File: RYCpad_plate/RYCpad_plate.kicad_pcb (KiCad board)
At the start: 2 copper layers, 77.2 x 96.2 mm, 0 parts

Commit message: update plate "PCB" and produce gerber
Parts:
- added svg2mod (x2): G***, personal:RYCpad_plate_coppertrim, F.Cu at (0.00, 9.50)
- added svg2mod (x2): G***, personal:RYCpad_plate_coppertrim, B.Cu at (0.00, 9.50)
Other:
- board text added: "RYCpad Plate v1.0"

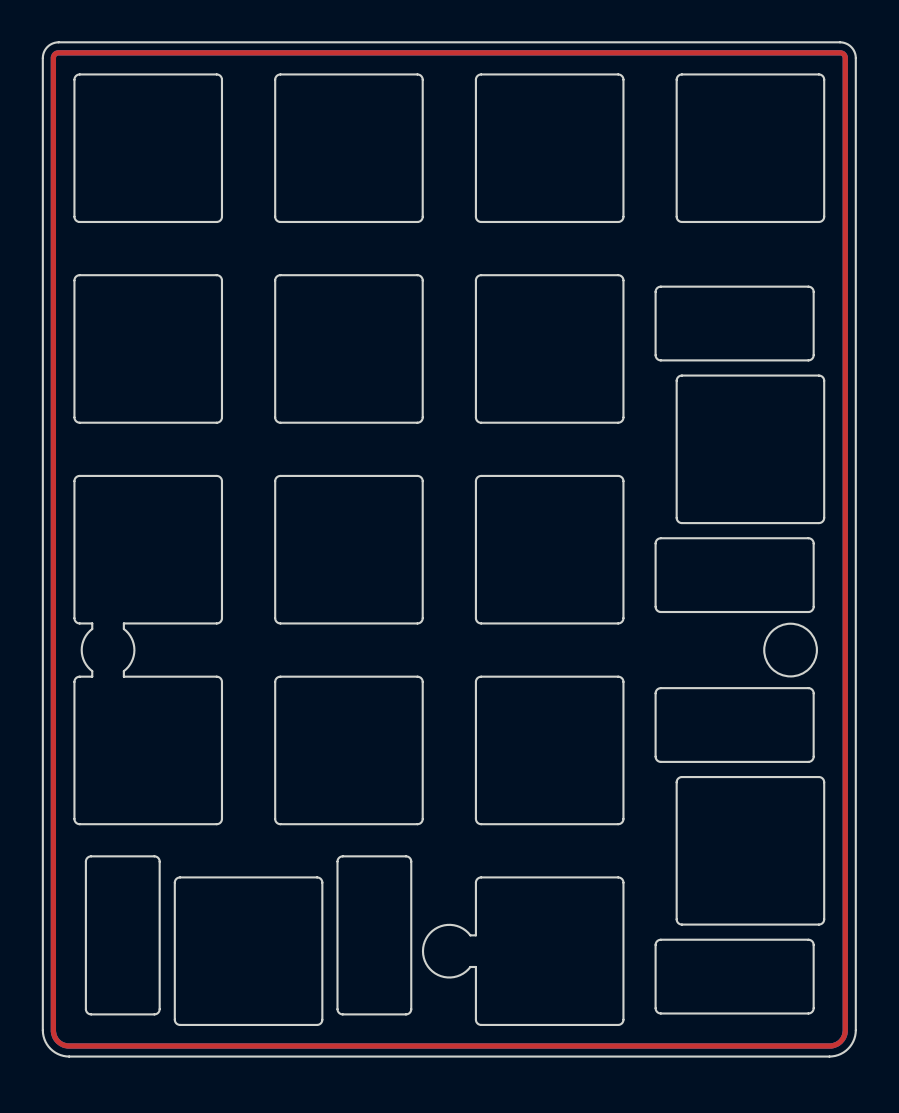
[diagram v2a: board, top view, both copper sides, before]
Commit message: add copper pour to plate
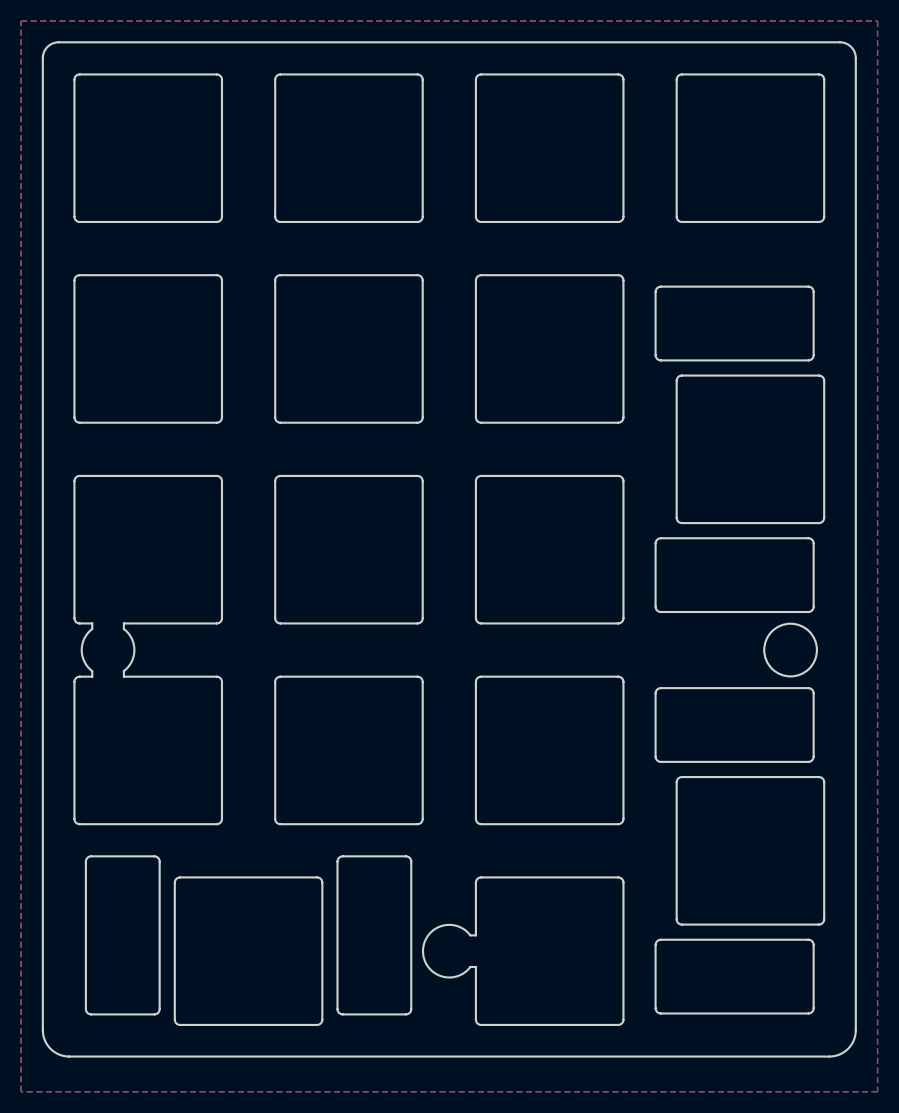
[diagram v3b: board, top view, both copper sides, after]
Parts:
- removed the svg2mod at (0.00, 9.50) (x2)
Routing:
- added copper zone on B.Cu, net (none)
- added copper zone on F.Cu, net (none)

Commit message: added more decoration to plate
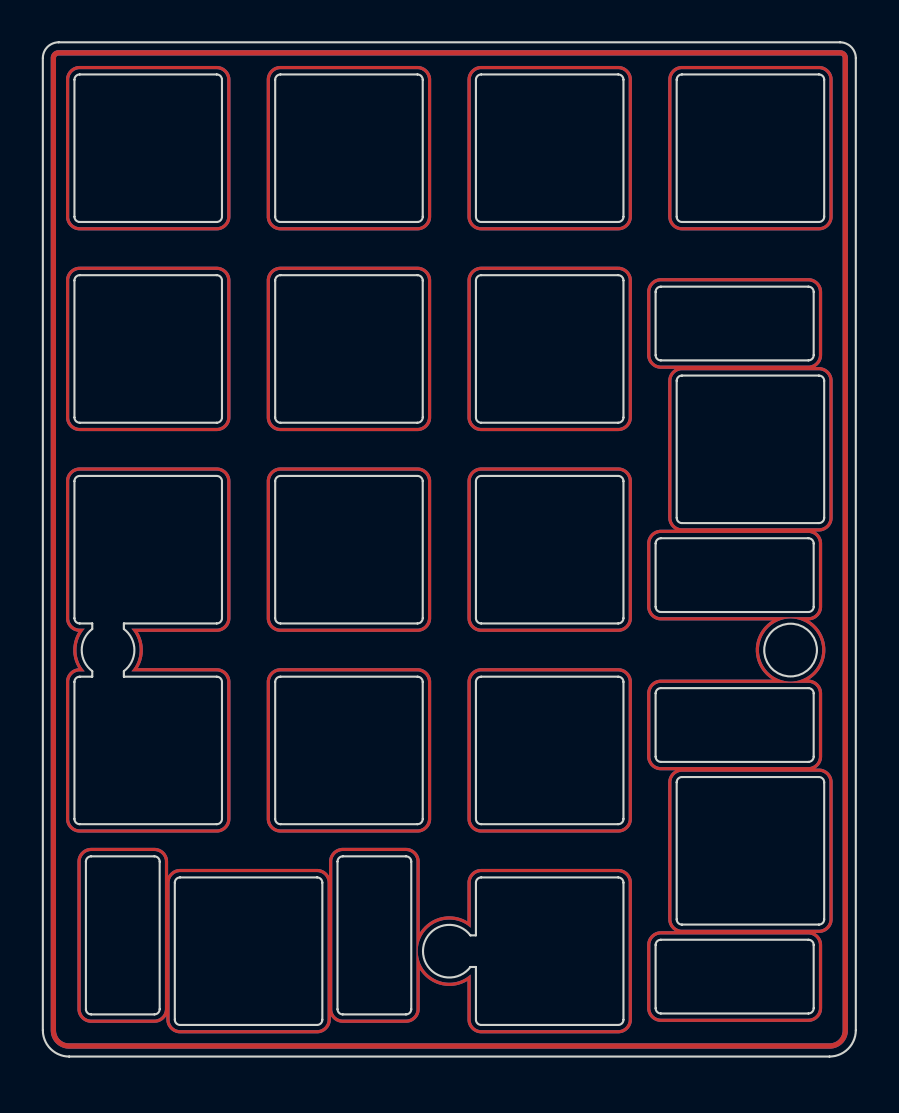
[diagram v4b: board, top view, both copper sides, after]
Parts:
- added svg2mod (x4): G***, personal:RYCpad_plate_switchtrim, F.Cu at (0.00, 9.52)
- added svg2mod: G***, personal:RYCpad_plate_coppertrim, F.Cu at (0.00, 9.50)
- added svg2mod: G***, personal:RYCpad_plate_coppertrim, B.Cu at (0.00, 9.50)
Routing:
- removed copper zone on B.Cu, net (none)
- removed copper zone on F.Cu, net (none)

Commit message: adjusted component cover and plate
- Old plate geometry would collide with IC socket
- Component cover lower edge pushed to show bottom edges of components
  more clearly
- Plate upper edge pushed to eliminate collision with IC socket
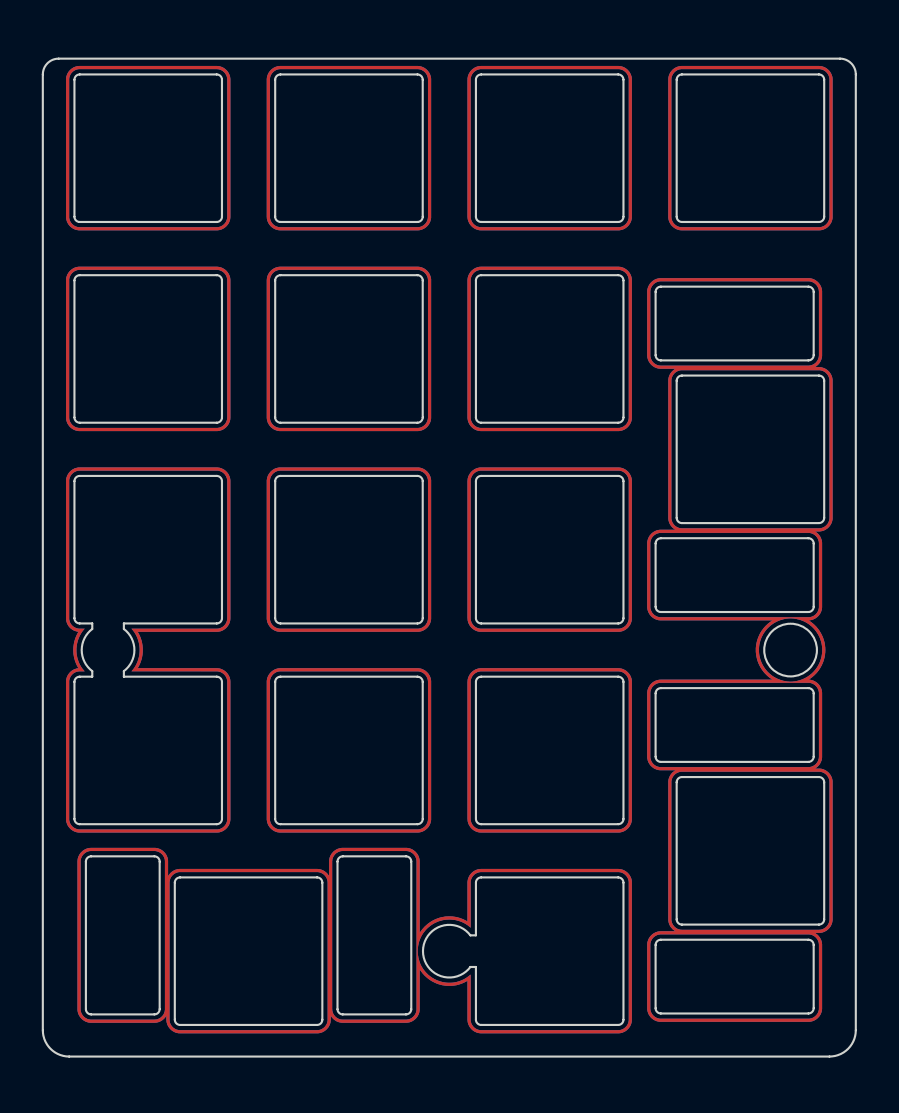
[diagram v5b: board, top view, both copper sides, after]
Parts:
- removed the svg2mod at (0.00, 9.50) (x4)
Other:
- board size 77.2 x 96.2 mm -> 77.2 x 94.7 mm
